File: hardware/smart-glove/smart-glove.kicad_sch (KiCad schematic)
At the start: 30 parts, among them J1 USB-C, J2 FLEX, J3 LiPo, SW1 BOOT, SW2 EN, U1 ESP32-WROOM-32E, U2 TP4056, U3 AMS1117-3.3, U4 MPU-6050

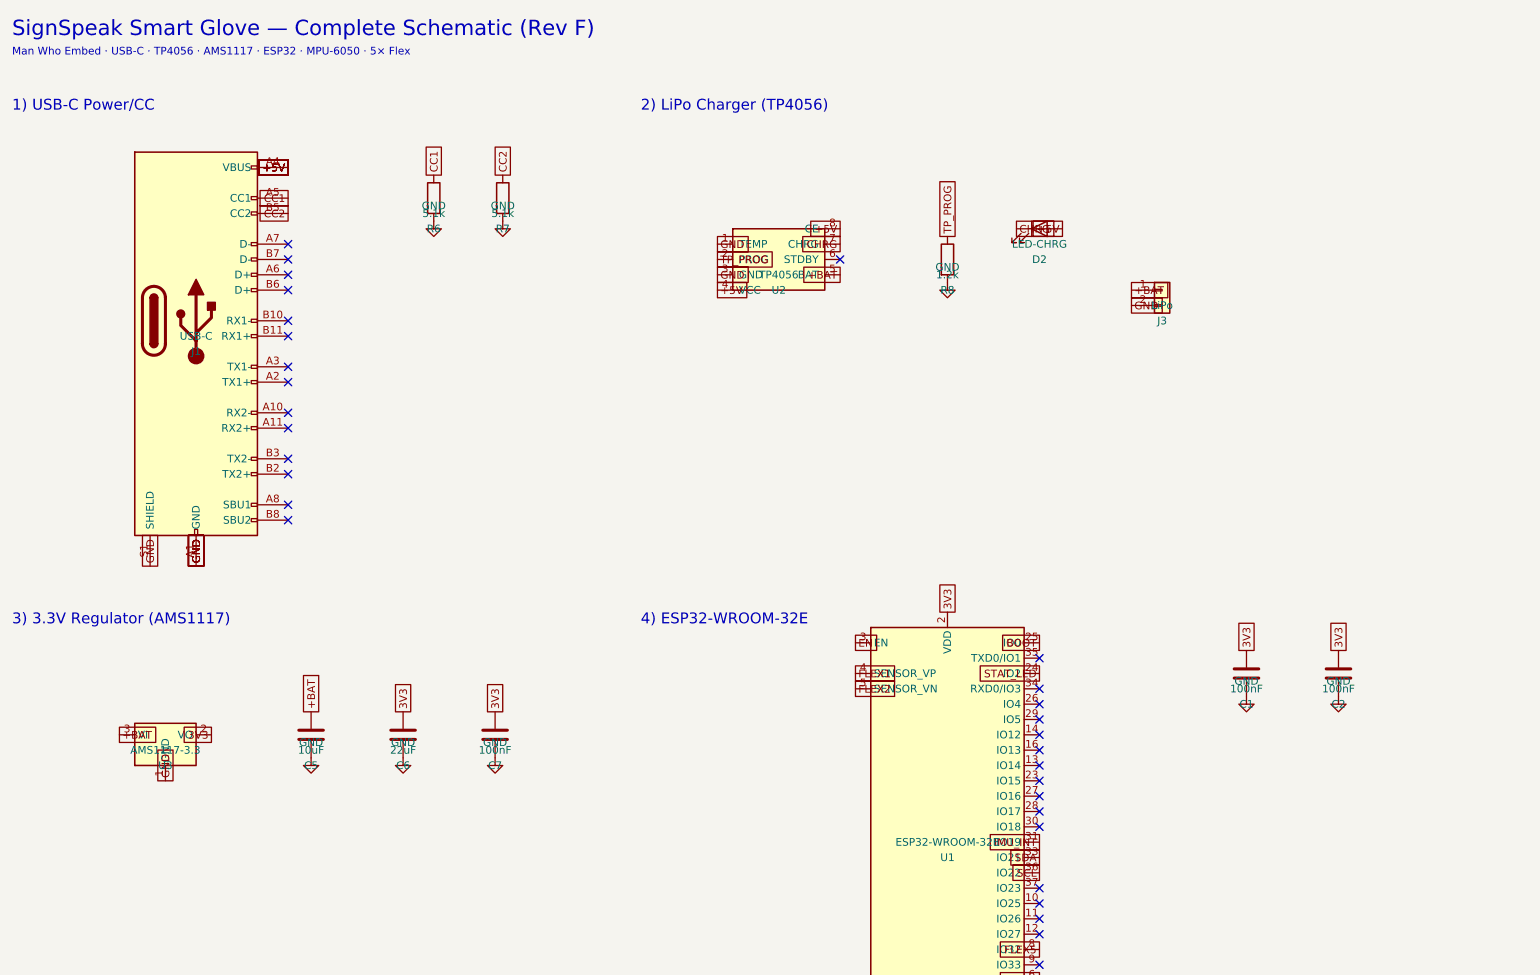
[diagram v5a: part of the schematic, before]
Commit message: Rev G: add UART prog header J4, shrink board to 60×45 mm
40×30 mm is not feasible with ESP32-WROOM-32E + USB-C + charger/IMU.
J4 1×4 (3V3/TX/RX/GND) enables USB-UART dongle flashing. DRC gate PASS.

Co-authored-by: ADIL ZAHOOR  <adilzahoor2812@users.noreply.github.com>
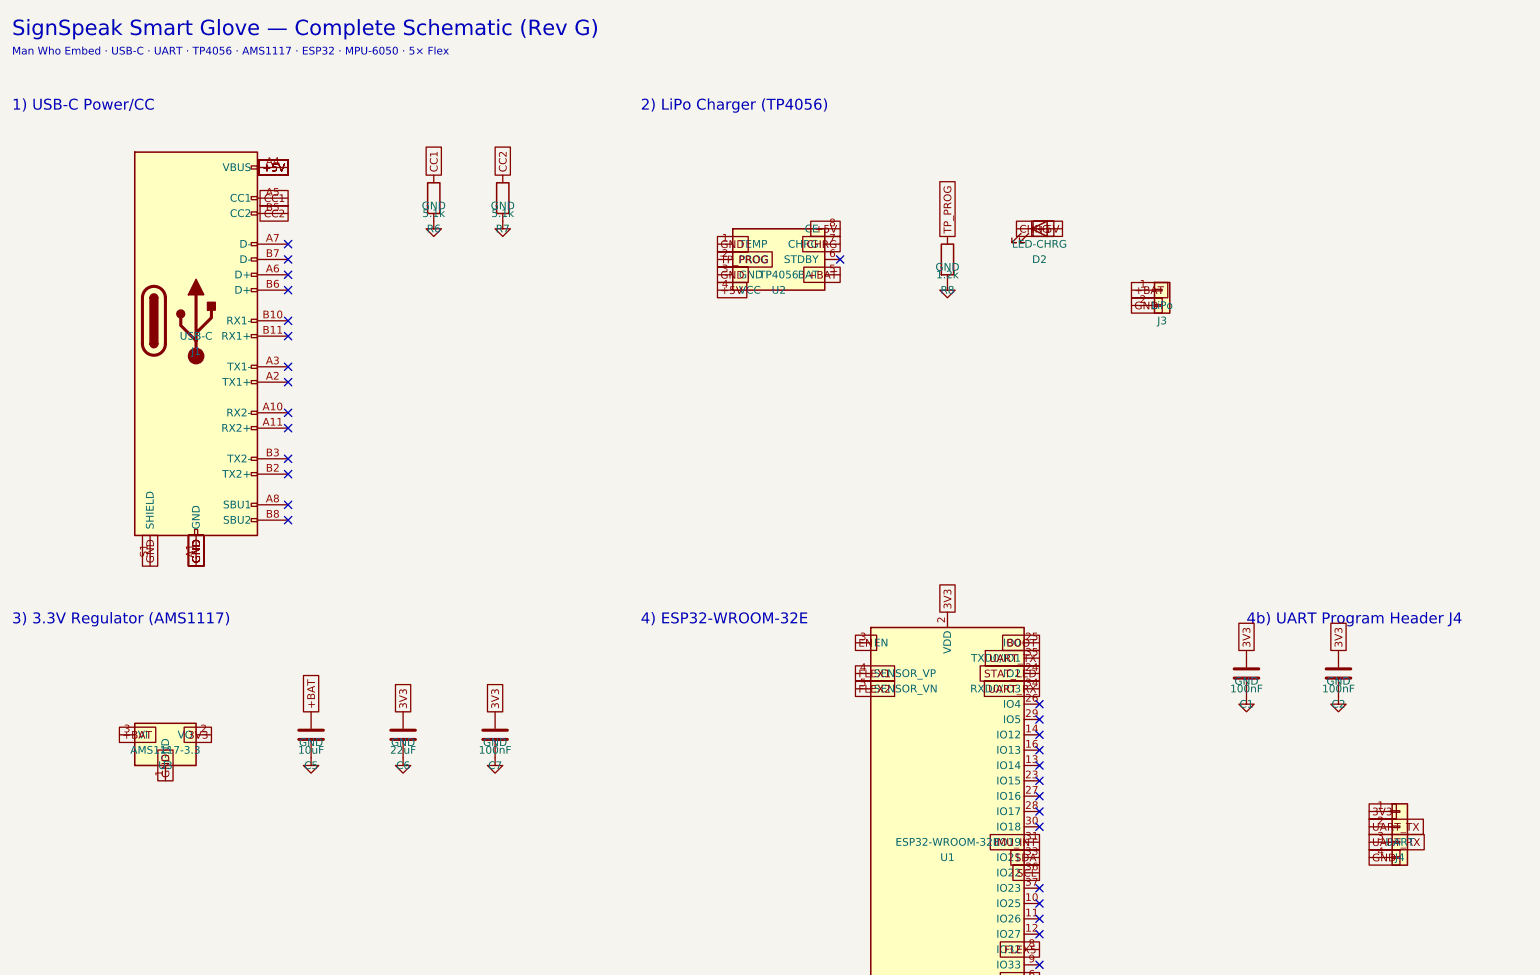
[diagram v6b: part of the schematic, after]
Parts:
- added J4: UART, Connector_PinHeader_2.54mm:PinHeader_1x04_P2.54mm_Vertical, symbol Connector_Generic:Conn_01x04
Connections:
- net 3V3: now also J4.1 (Pin_1)
- net GND: now also J4.4 (Pin_4)
- net UART_RX: now reaches U1.34 (RXD0/IO3)
- net UART_RX: now also J4.3 (Pin_3)
- net UART_TX: now reaches U1.35 (TXD0/IO1)
- net UART_TX: now also J4.2 (Pin_2)
- no-connect marks 36 -> 34
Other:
- note added: "4b) UART Program Header J4"
- note added: "Man Who Embed · USB-C · UART · TP4056 · AMS1117 · ESP32 · MPU-6050 · 5× Flex"
- note added: "SignSpeak Smart Glove — Complete Schematic (Rev G)"
- note removed: "Man Who Embed · USB-C · TP4056 · AMS1117 · ESP32 · MPU-6050 · 5× Flex"
- note removed: "SignSpeak Smart Glove — Complete Schematic (Rev F)"
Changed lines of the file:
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@@
     (title "SignSpeak Smart Glove")
     (date "2026-07-18")
-    (rev "F")
+    (rev "G")
     (company "Man Who Embed")
-    (comment 1 "5× flex · ESP32 · TP4056 · AMS1117 · MPU-6050 · USB-C")
-  )
-  (text "SignSpeak Smart Glove — Complete Schematic (Rev F)" (exclude_from_sim no) (at 25.4 12.7 0) (effects (font (size 2.54 2.54)) (justify left))
-  )
-  (text "Man Who Embed · USB-C · TP4056 · AMS1117 · ESP32 · MPU-6050 · 5× Flex" (exclude_from_sim no) (at 25.4 16.51 0) (effects (font (size 1.27 1.27)) (justify left))
+    (comment 1 "5× flex · ESP32 · UART prog · TP4056 · AMS1117 · MPU-6050 · USB-C")
+  )
+  (text "SignSpeak Smart Glove — Complete Schematic (Rev G)" (exclude_from_sim no) (at 25.4 12.7 0) (effects (font (size 2.54 2.54)) (justify left))
+  )
+  (text "Man Who Embed · USB-C · UART · TP4056 · AMS1117 · ESP32 · MPU-6050 · 5× Flex" (exclude_from_sim no) (at 25.4 16.51 0) (effects (font (size 1.27 1.27)) (justify left))
   )
   (text "1) USB-C Power/CC" (exclude_from_sim no) (at 25.4 25.4 0) (effects (font (size 1.8 1.8)) (justify left))
@@
   (global_label "SDA" (shape passive) (at 195.58 149.86 180) (effects (font (size 1.27 1.27)) (justify right))
   )
+  (global_label "UART_RX" (shape passive) (at 195.58 121.92 180) (effects (font (size 1.27 1.27)) (justify right))
+  )
+  (global_label "UART_TX" (shape passive) (at 195.58 116.84 180) (effects (font (size 1.27 1.27)) (justify right))
+  )
   (global_label "SCL" (shape passive) (at 195.58 152.4 180) (effects (font (size 1.27 1.27)) (justify right))
   )
@@
   (no_connect (at 195.58 127.0))
   (no_connect (at 195.58 144.78))
-  (no_connect (at 195.58 121.92))
-  (no_connect (at 195.58 116.84))
   (no_connect (at 195.58 154.94))
+  (text "4b) UART Program Header J4" (exclude_from_sim no) (at 229.87 110.49 0) (effects (font (size 1.8 1.8)) (justify left))
+  )
+  (symbol (lib_id "Connector_Generic:Conn_01x04") (at 255.27 144.78 0) (unit 1) (in_bom yes) (on_board yes) (dnp no)
+    (property "Reference" "J4" (at 255.27 149.86 0) (effects (font (size 1.27 1.27))))
+    (property "Value" "UART" (at 255.27 147.32 0) (effects (font (size 1.27 1.27))))
+    (property "Footprint" "Connector_PinHeader_2.54mm:PinHeader_1x04_P2.54mm_Vertical" (at 255.27 144.78 0) (effects (font (size 1.27 1.27)) hide))
+    (property "Datasheet" "" (at 255.27 144.78 0) (effects (font (size 1.27 1.27)) hide))
+  )
+  (global_label "3V3" (shape passive) (at 250.19 142.24 0) (effects (font (size 1.27 1.27)) (justify left))
+  )
+  (global_label "UART_TX" (shape passive) (at 250.19 144.78 0) (effects (font (size 1.27 1.27)) (justify left))
+  )
+  (global_label "UART_RX" (shape passive) (at 250.19 147.32 0) (effects (font (size 1.27 1.27)) (justify left))
+  )
+  (global_label "GND" (shape passive) (at 250.19 149.86 0) (effects (font (size 1.27 1.27)) (justify left))
+  )
   (symbol (lib_id "Device:C") (at 229.87 119.38 0) (unit 1) (in_bom yes) (on_board yes) (dnp no)
     (property "Reference" "C1" (at 229.87 124.46 0) (effects (font (size 1.27 1.27))))

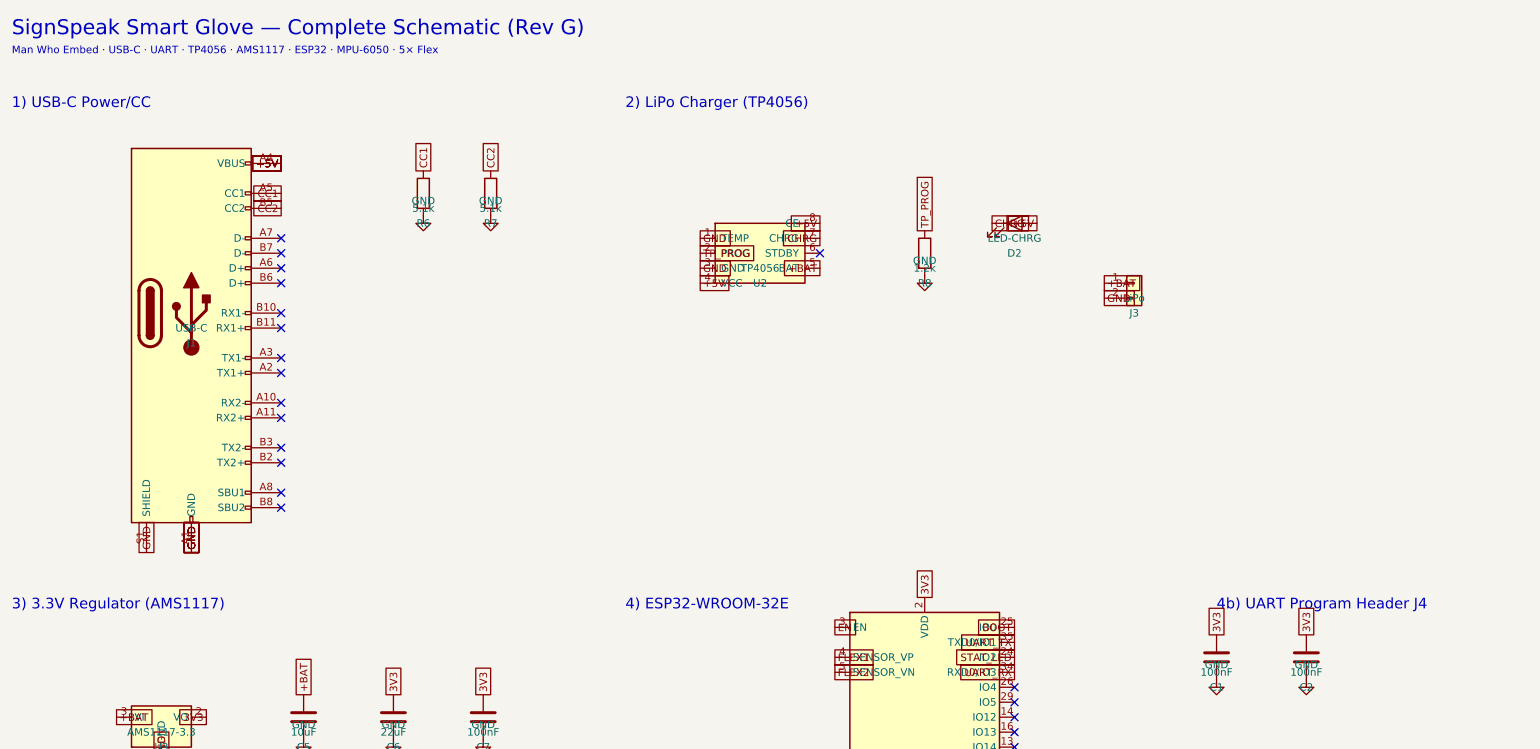
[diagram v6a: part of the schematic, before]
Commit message: Rev H: USB-C CH340, LiPo protect, firmware, compliance package
Resolves production gaps: onboard USB serial (CH340), DW01+FS8205
battery protection, RF mounting guide, LCSC BOM, assembly notes,
compliance path docs, and SignSpeak Arduino firmware with serial CSV.

Co-authored-by: ADIL ZAHOOR  <adilzahoor2812@users.noreply.github.com>
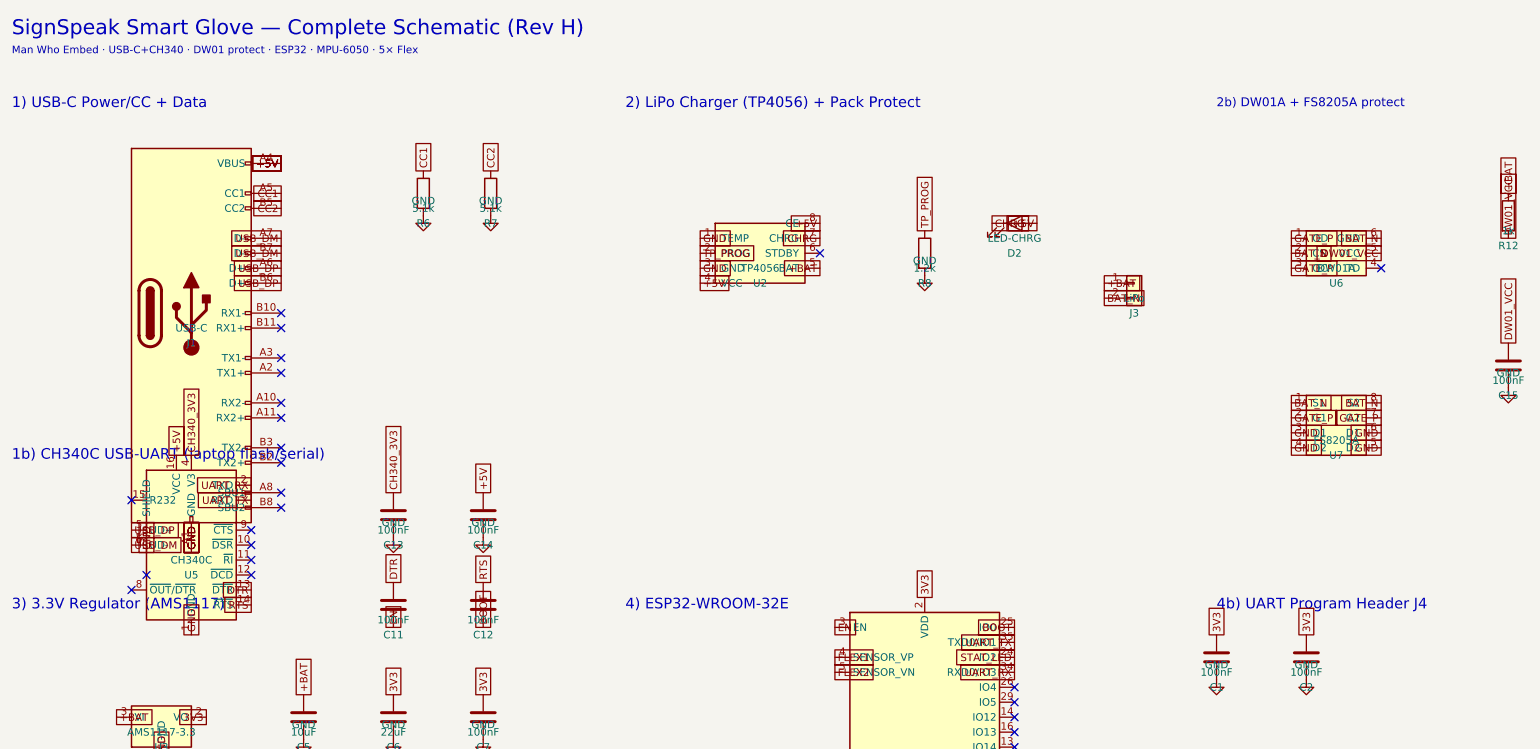
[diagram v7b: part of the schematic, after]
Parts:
- added C11, C12, C13, C14, C15: 100nF, Capacitor_SMD:C_0603_1608Metric, symbol Device:C
- added R12: 1k, Resistor_SMD:R_0603_1608Metric, symbol Device:R
- added U5: CH340C, Package_SO:SOIC-16_3.9x9.9mm_P1.27mm, symbol Interface_USB:CH340C
- added U6: DW01A, Package_TO_SOT_SMD:SOT-23-6, symbol Device:DW01A
- added U7: FS8205A, Package_SO:TSSOP-8_3x3mm_P0.65mm, symbol Device:FS8205A
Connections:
- net +5V: now also C14.1, U5.16 (VCC)
- net +BAT: now also R12.1
- net BOOT: now also C12.2
- net EN: now also C11.2
- net GND: now also C13.2, C14.2, C15.2, U5.1 (GND), U7.3 (D1), U7.4 (D2), U7.5 (D2), U7.6 (D1); no longer J3.2 (Pin_2)
- net UART_RX: now also U5.2 (TXD)
- net UART_TX: now also U5.3 (RXD)
- net USB_DP: now reaches J1.A6 (D+)
- net USB_DP: now also J1.B6 (D+), U5.5 (UD+)
- net USB_DM: now reaches J1.A7 (D-)
- net USB_DM: now also J1.B7 (D-), U5.6 (UD-)
- new net BAT_N: J3.2 (Pin_2), U6.2 (CS), U6.6 (GND), U7.1 (S1), U7.8 (S2)
- new net CH340_3V3: C13.1, U5.4 (V3)
- new net DTR: C11.1, U5.13 (~{DTR})
- new net DW01_VCC: C15.1, R12.2, U6.5 (VCC)
- new net GATE_P: U6.1 (OD), U6.3 (OC), U7.2 (G1), U7.7 (G2)
- new net RTS: C12.1, U5.14 (~{RTS})
- no-connect marks 34 -> 38
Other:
- note added: "1) USB-C Power/CC + Data"
- note added: "1b) CH340C USB-UART (laptop flash/serial)"
- note added: "2) LiPo Charger (TP4056) + Pack Protect"
- note added: "2b) DW01A + FS8205A protect"
- note added: "Man Who Embed · USB-C+CH340 · DW01 protect · ESP32 · MPU-6050 · 5× Flex"
- note added: "SignSpeak Smart Glove — Complete Schematic (Rev H)"
- note removed: "1) USB-C Power/CC"
- note removed: "2) LiPo Charger (TP4056)"
- note removed: "Man Who Embed · USB-C · UART · TP4056 · AMS1117 · ESP32 · MPU-6050 · 5× Flex"
- note removed: "SignSpeak Smart Glove — Complete Schematic (Rev G)"

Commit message: Restyle SignSpeak schematic into labeled functional blocks
Match professional ESP32 board schematic layout style (dashed
section boxes + titled zones) while keeping Rev H SignSpeak
nets and parts. ERC: 0 errors.

Co-authored-by: ADIL ZAHOOR  <adilzahoor2812@users.noreply.github.com>
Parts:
- C10: footprint Capacitor_SMD:C_0603_1608Metric -> Capacitor_SMD:C_0805_2012Metric
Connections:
- no-connect marks 38 -> 37
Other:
- note added: "1=3V3 2=TX 3=RX 4=GND"
- note added: "Addr 0x68 · SDA=IO21 · SCL=IO22"
- note added: "Auto-program caps → EN / BOOT"
- note added: "Battery Pack Protect (DW01A + FS8205A):"
- note added: "D1 = power · D3 = ESP32 IO2 status"
- note added: "ESP32 Reset & Boot circuit:"
- note added: "ESP32-WROOM-32E:"
- note added: "Flex Sensors (5×) + Dividers:"
- note added: "IMU (MPU-6050) I2C:"
- note added: "J2: 3V3 · FLEX1..5 · GND"
- note added: "LiPo Charger (TP4056):"
- note added: "POWER AND STATUS LED's:"
- note added: "POWER SUPPLY (BAT to 3V3):"
- note added: "UART Program Header:"
- note added: "USB TO UART BRIDGE (CH340C):"
- note added: "USB-C Connector & CC:"
- note removed: "1) USB-C Power/CC + Data"
- note removed: "1b) CH340C USB-UART (laptop flash/serial)"
- note removed: "2) LiPo Charger (TP4056) + Pack Protect"
- note removed: "2b) DW01A + FS8205A protect"
- note removed: "3) 3.3V Regulator (AMS1117)"
- note removed: "4) ESP32-WROOM-32E"
- note removed: "4b) UART Program Header J4"
- note removed: "5) BOOT / EN / Status LEDs"
- note removed: "6) Flex Sensor Header + Dividers (5×)"
- note removed: "7) IMU MPU-6050"
- note removed: "Man Who Embed · USB-C+CH340 · DW01 protect · ESP32 · MPU-6050 · 5× Flex"
- note removed: "Power flags (ERC)"
- note removed: "SignSpeak Smart Glove — Complete Schematic (Rev H)"
